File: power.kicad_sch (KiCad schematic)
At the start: 20 parts, among them J1 Conn_01x02, J5 USB_B_Micro, SW1 SW_SPDT, U1 LDO 3V3, U1 LTC4054ES5-4.2, U2 XB330xS

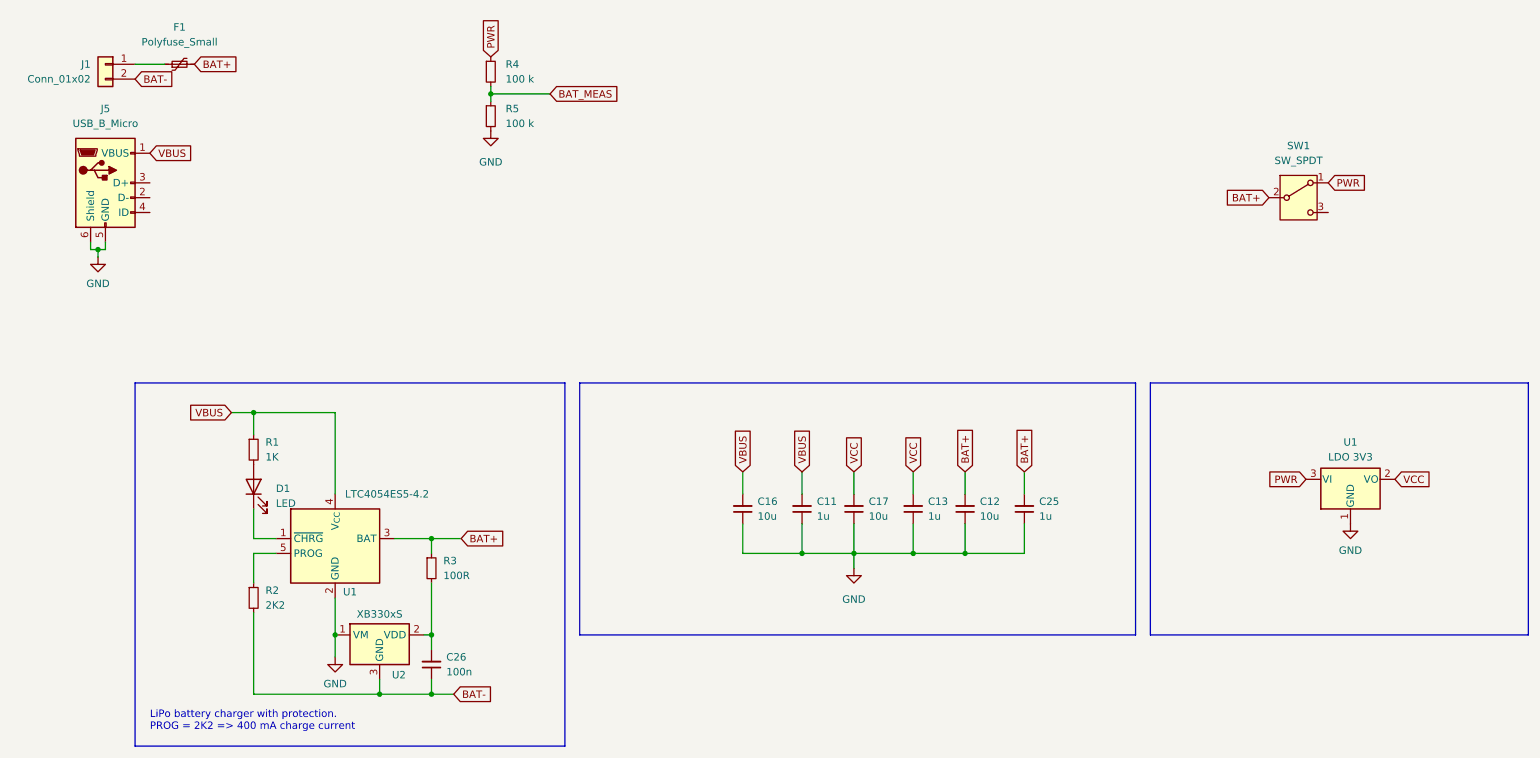
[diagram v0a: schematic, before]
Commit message: Fix power on debug connector
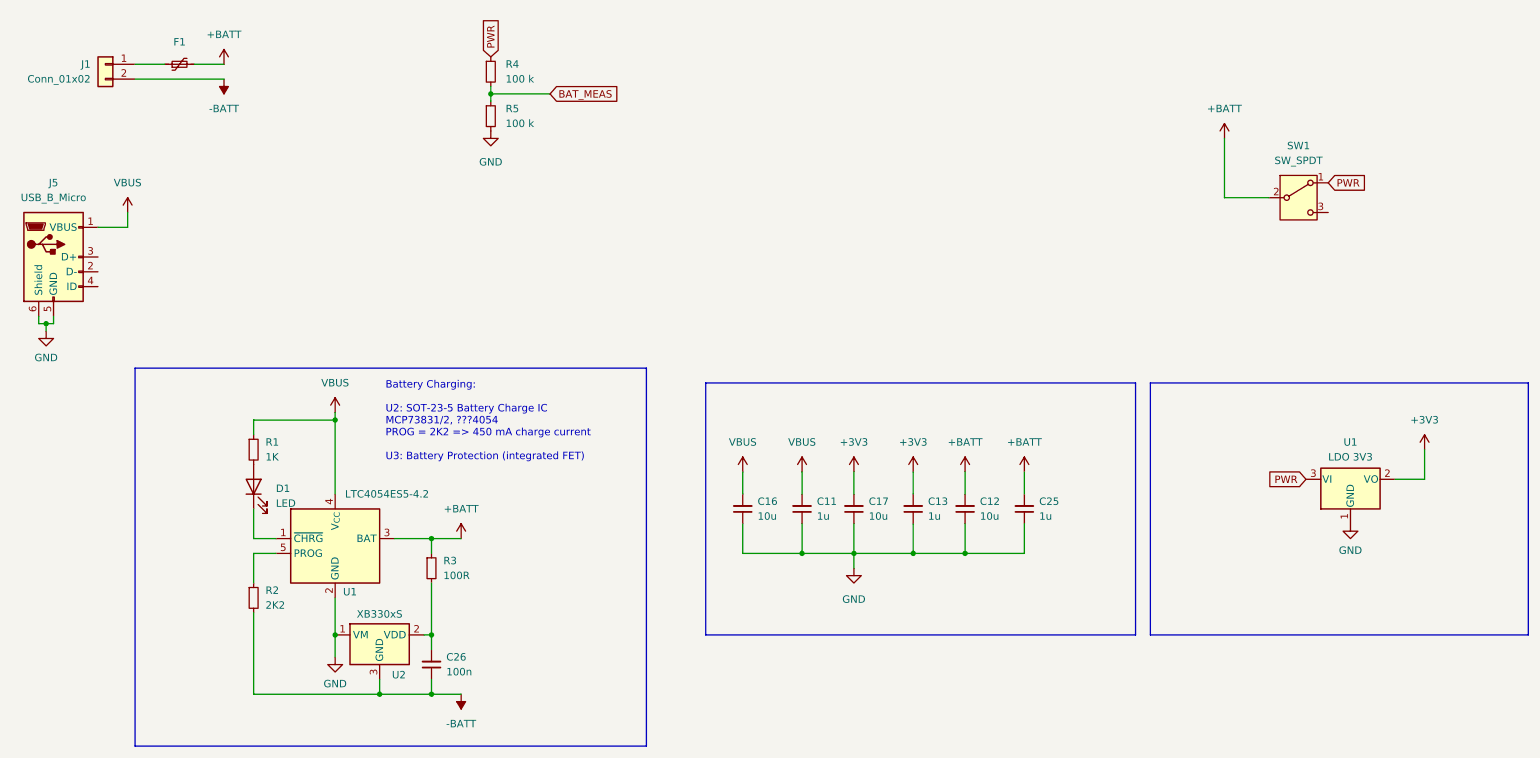
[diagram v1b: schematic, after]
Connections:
- net BAT+ renamed +BATT
- net BAT- renamed -BATT
- net VCC renamed +3V3
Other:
- note added: "Battery Charging: U2: SOT-23-5 Battery Charge IC MCP73831/2, ???4054 PROG = 2K2 => 450 mA charge current U3: Battery Protection (integrated FET)"
- note removed: "LiPo battery charger with protection. PROG = 2K2 => 400 mA charge current"
- moved on the sheet: J5
